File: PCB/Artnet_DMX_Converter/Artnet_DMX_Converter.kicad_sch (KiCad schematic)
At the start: 4 parts

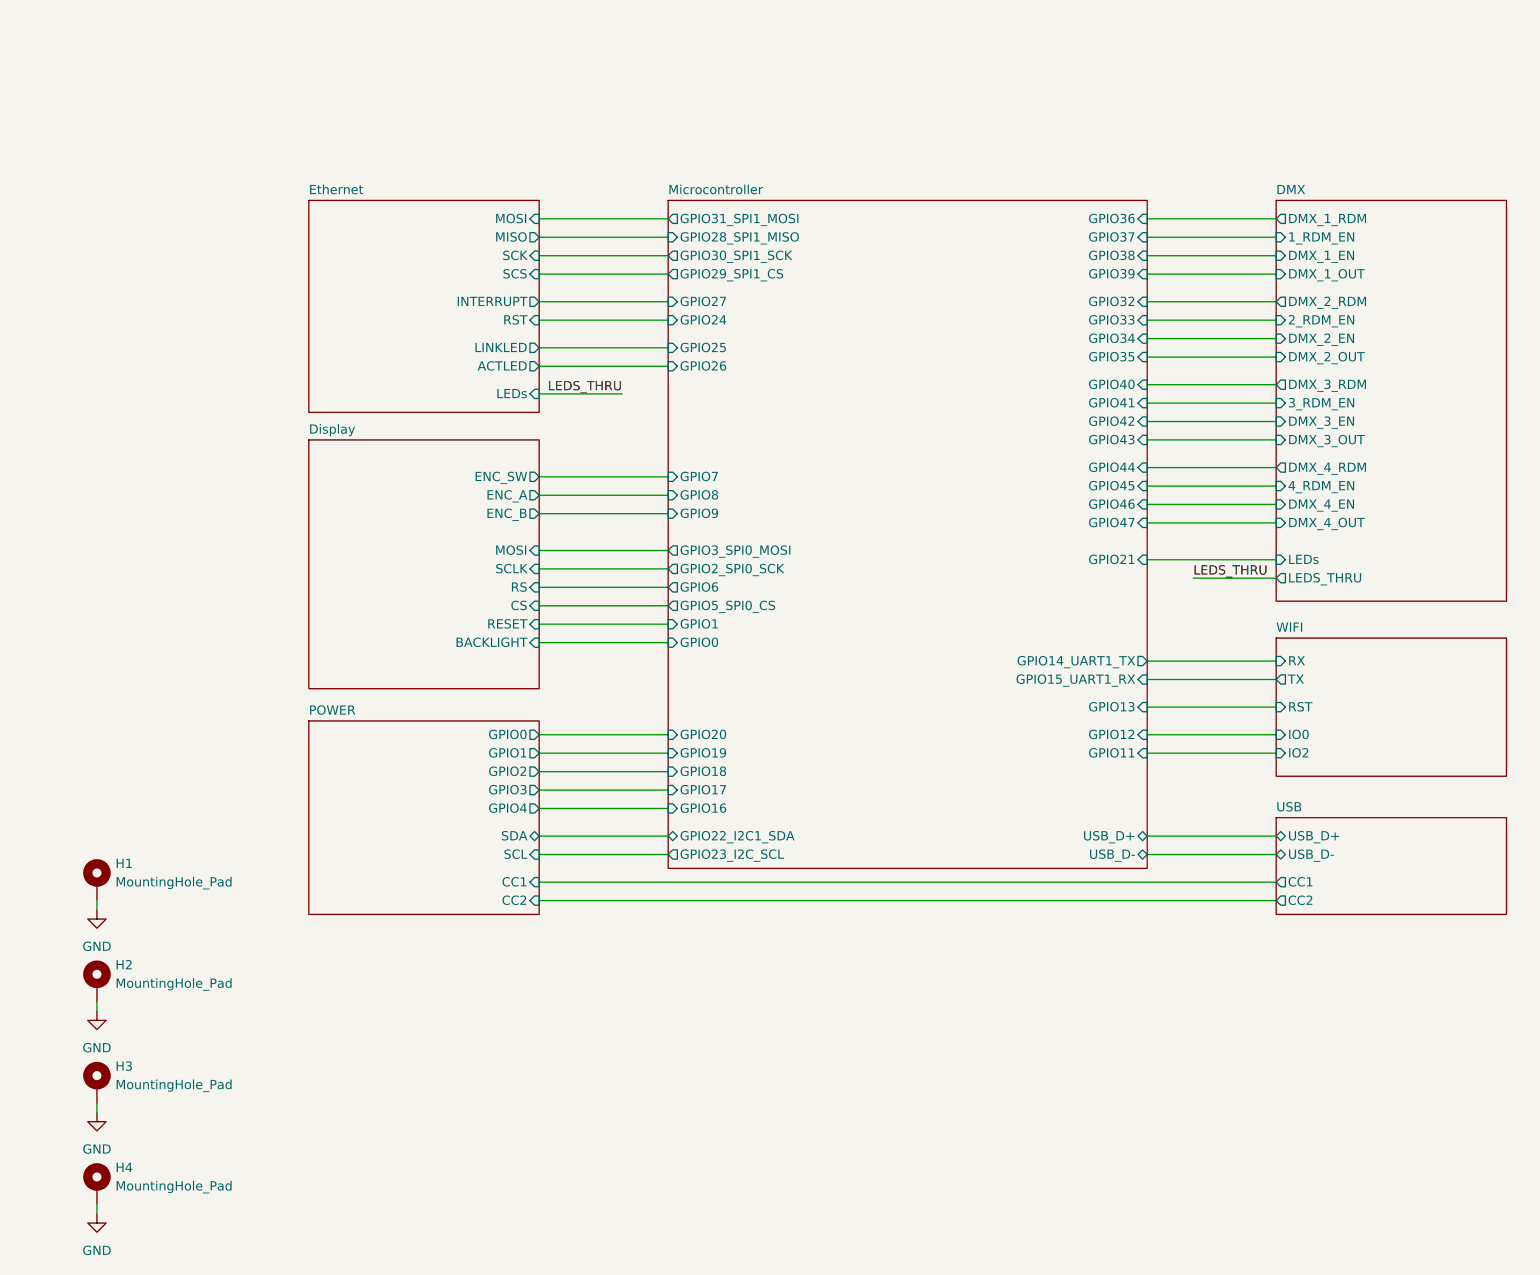
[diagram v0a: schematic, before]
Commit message: Updated the PCB Allot
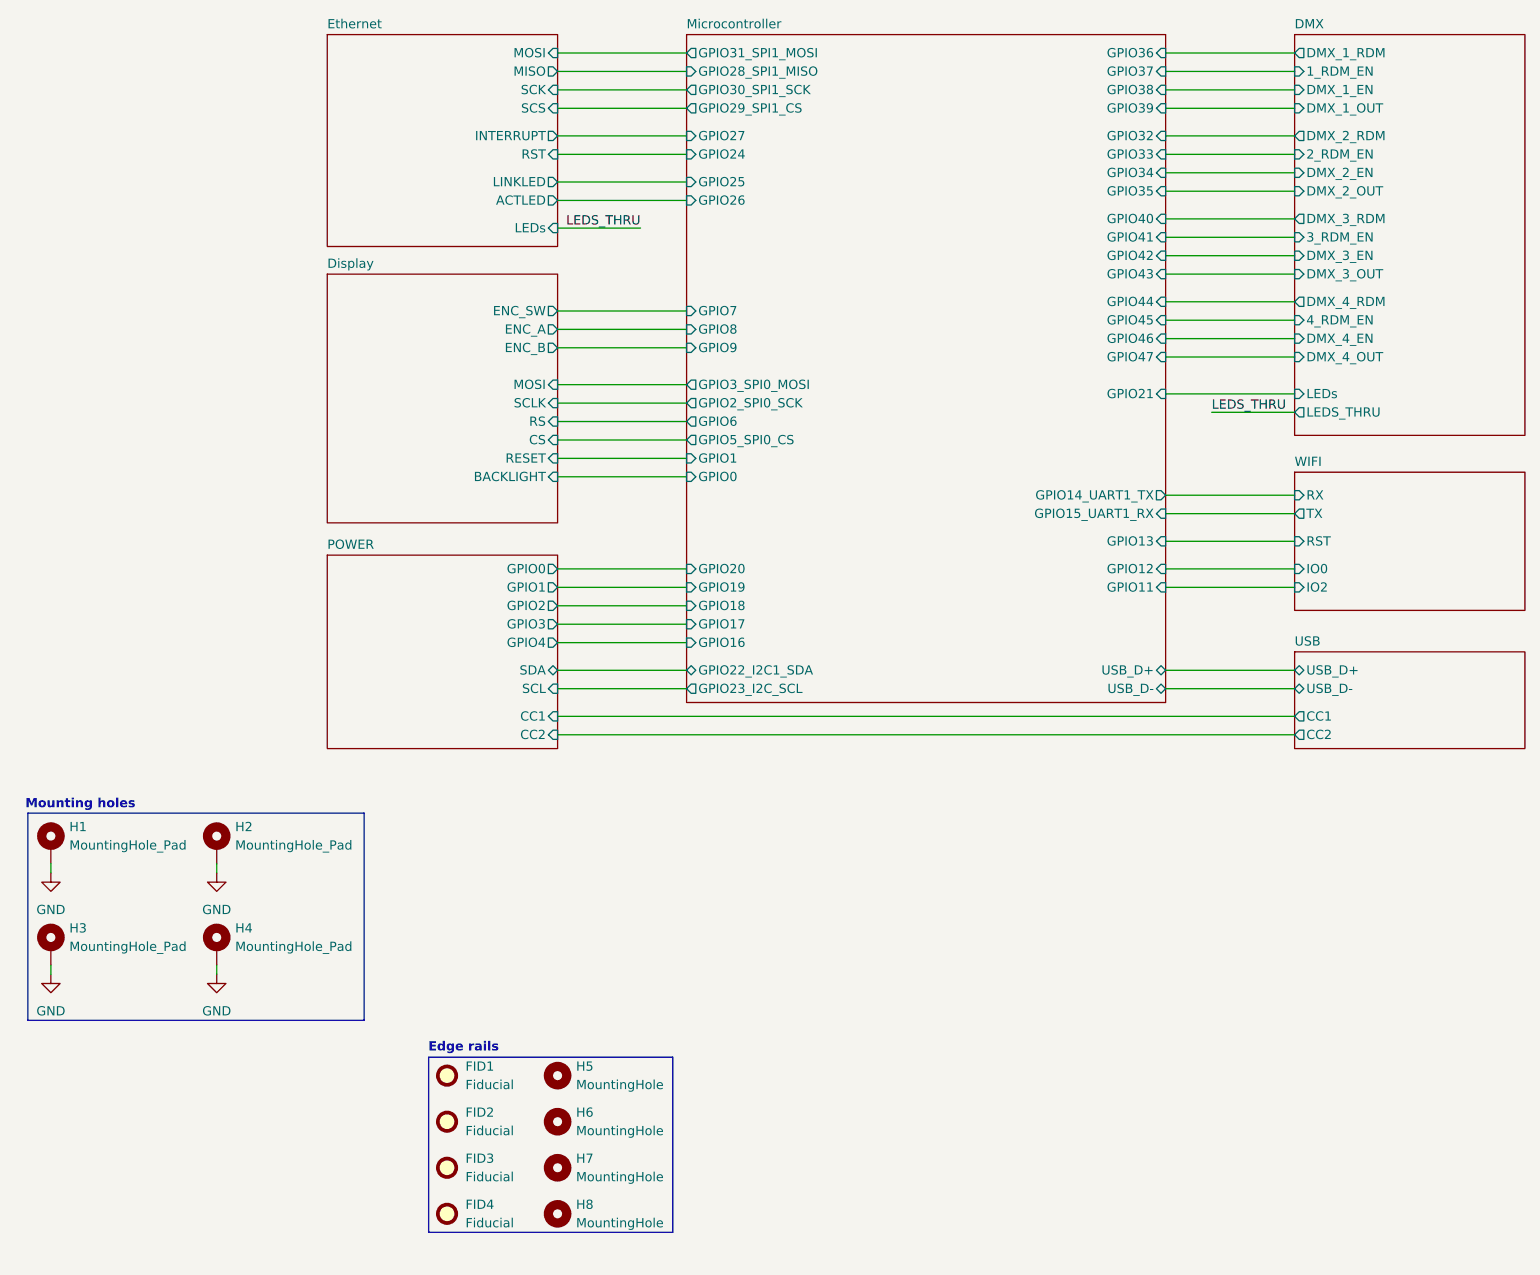
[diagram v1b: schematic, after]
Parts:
- added FID1, FID2, FID3, FID4: Fiducial, Fiducial:Fiducial_1mm_Mask2mm, symbol Mechanical:Fiducial
- added H5, H6, H7, H8: MountingHole, MountingHole:MountingHole_2mm, symbol Mechanical:MountingHole
- renumbered H3 to H2, H2 to H3
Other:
- note added: "Edge rails"
- note added: "Mounting holes"
- moved on the sheet: H1, H2, H3, H4
